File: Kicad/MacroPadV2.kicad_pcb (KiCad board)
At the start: 2 copper layers, 81 x 70 mm, 26 parts, among them K1 KSW, K10 KSW, K11 KSW, K12 KSW, K2 KSW, K3 KSW, K4 KSW, K5 KSW, K6 KSW, K7 KSW, K8 KSW, K9 KSW, SW1 RotaryEncoder_Switch, U1 SparkFunProMicro

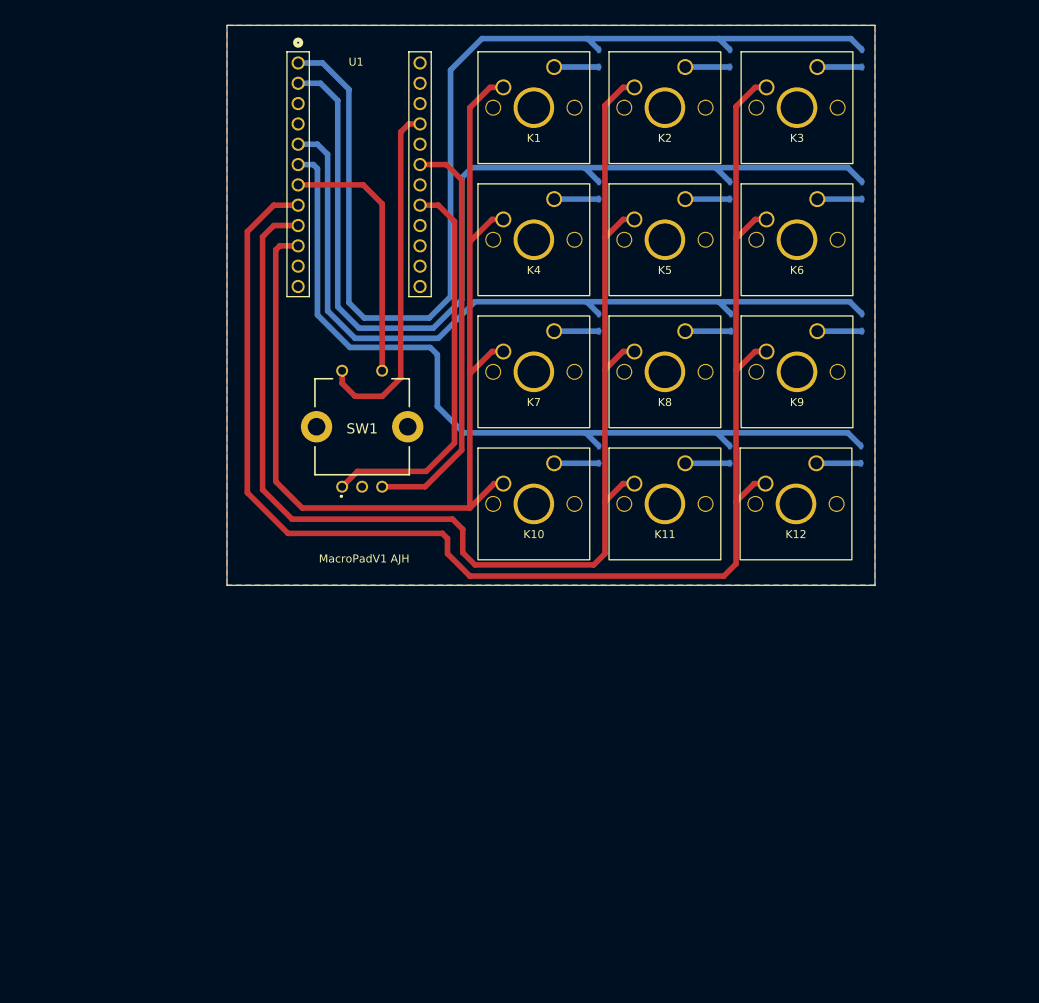
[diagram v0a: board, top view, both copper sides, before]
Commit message: Started V2 	-More space between keys(keycaps didnt fit) 	-Pull Down Resistors for Columns and Rotary Switch(ATMega32U4 is internal pull up) 	-Slightly larger board and edge holes
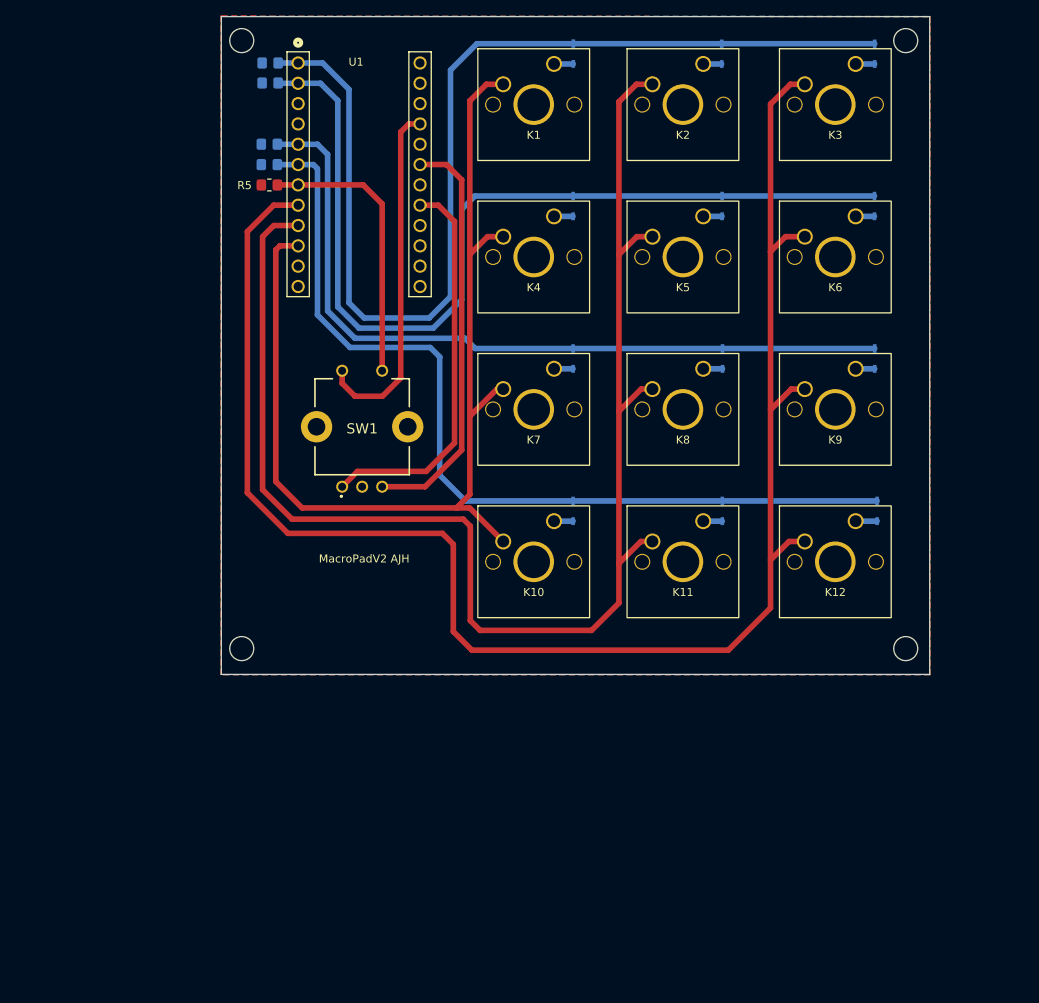
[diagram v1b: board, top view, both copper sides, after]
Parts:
- added R1: 1k, Resistor_SMD:R_0805_2012Metric_Pad1.20x1.40mm_HandSolder, B.Cu at (39.5, 26.8)
- added R2: 1k, Resistor_SMD:R_0805_2012Metric_Pad1.20x1.40mm_HandSolder, B.Cu at (39.5, 29.3)
- added R3: 1k, Resistor_SMD:R_0805_2012Metric_Pad1.20x1.40mm_HandSolder, B.Cu at (39.5, 37.0)
- added R4: 1k, Resistor_SMD:R_0805_2012Metric_Pad1.20x1.40mm_HandSolder, B.Cu at (39.5, 39.5)
- added R5: 1k, Resistor_SMD:R_0805_2012Metric_Pad1.20x1.40mm_HandSolder, F.Cu at (39.5, 42.0)
- D1, D10, D11, D12, D2, D3, D4, D5, D6, D7, D8, D9: footprint aarohanl:CR_SOD323_MCC-L -> mpadfps:sod323
- moved K12 8.75 mm to (110.2, 89.2)
- moved K11 7.58 mm to (91.2, 89.2)
- moved K10 7.24 mm to (72.5, 89.2)
- moved D10 6.82 mm to (77.4, 81.8)
- moved K9 6.71 mm to (110.2, 70.1)
- moved D12 6.34 mm to (115.4, 81.8)
- moved D11 6.09 mm to (96.1, 81.8)
- moved K6 5.25 mm to (110.2, 51.0)
- moved K8 5.21 mm to (91.2, 70.1)
- moved K3 4.81 mm to (110.2, 32.0)
- moved D7 4.74 mm to (77.4, 62.7)
- moved K7 4.70 mm to (72.5, 70.1)
- moved D9 3.82 mm to (115.1, 62.7)
- moved D8 3.63 mm to (96.1, 62.7)
- moved D1 3.58 mm to (77.5, 24.6)
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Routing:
- net ROW2: track 183.7 -> 206.5 mm
- net ROW1: track 160.1 -> 180.3 mm
- net COL3: track 104.1 -> 111.8 mm
- net COL1: track 121.2 -> 115.8 mm
- net Net-(D8-Pad2): track 5.72 -> 2.41 mm
- net Net-(D2-Pad2): track 5.59 -> 2.31 mm
- net Net-(D5-Pad2): track 5.59 -> 2.36 mm
- net Net-(D6-Pad2): track 5.59 -> 2.36 mm
- net Net-(D11-Pad2): track 5.59 -> 2.39 mm
- net Net-(D7-Pad2): track 5.59 -> 2.39 mm
- net Net-(D10-Pad2): track 5.59 -> 2.39 mm
- net Net-(D3-Pad2): track 5.59 -> 2.39 mm
- net Net-(D9-Pad2): track 5.59 -> 2.39 mm
- net Net-(D4-Pad2): track 5.59 -> 2.39 mm
- net Net-(D1-Pad2): track 5.59 -> 2.41 mm
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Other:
- board size 81 x 70 mm -> 88.5 x 82.2 mm
- board text added: "MacroPadV2 AJH"
- board text removed: "MacroPadV1 AJH"

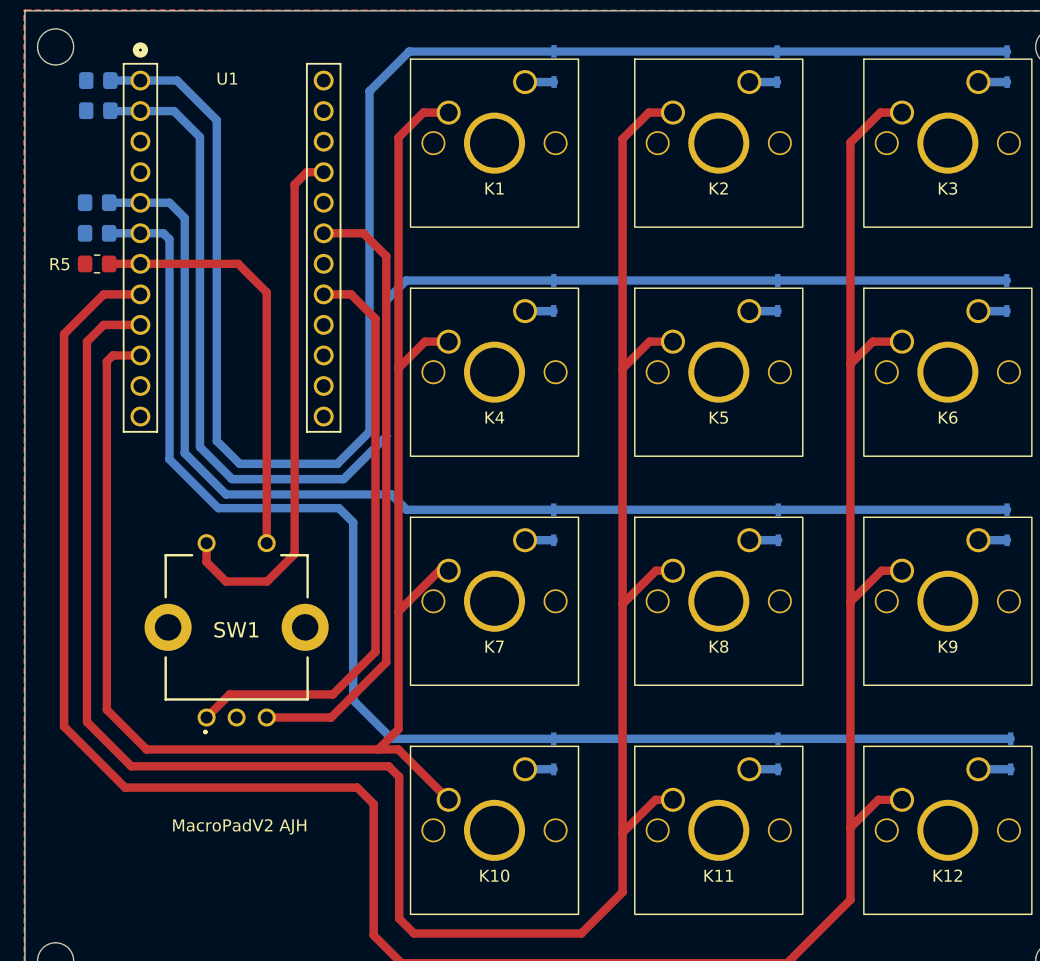
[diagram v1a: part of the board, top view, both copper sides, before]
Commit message: V2 Schem and Routing Complete for drop in micro pro, making new branch for STM32F103
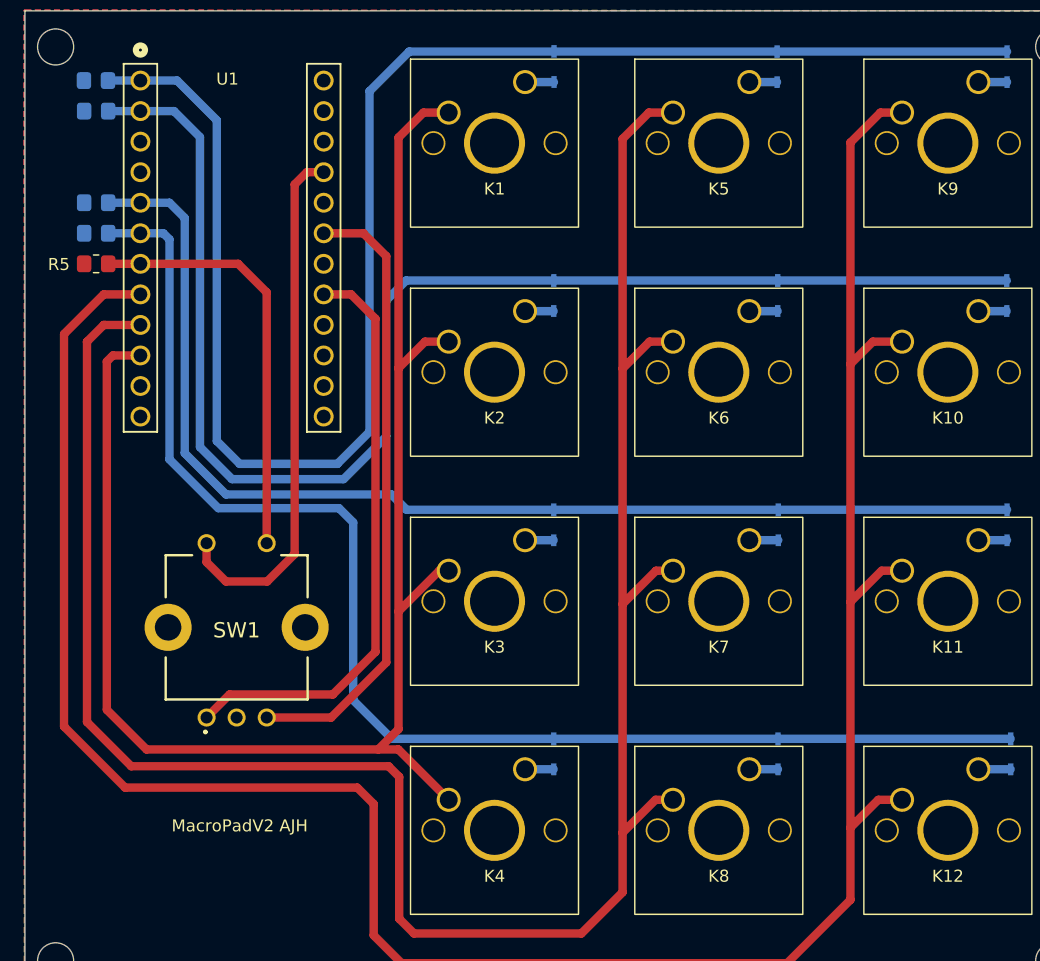
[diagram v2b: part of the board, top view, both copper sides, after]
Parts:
- moved R1 0.20 mm to (39.4, 26.8)
- moved R2 0.18 mm to (39.4, 29.3)
- moved R5 0.08 mm to (39.4, 42.0)
- moved R3 0.08 mm to (39.4, 37.0)
- moved R4 0.08 mm to (39.4, 39.5)
- renumbered D6 to D10, D9 to D11, D4 to D2, D7 to D3, D10 to D4, D2 to D5, D5 to D6, D8 to D7, D11 to D8, D3 to D9, K6 to K10, K9 to K11, K4 to K2, K7 to K3, K10 to K4, K2 to K5, K5 to K6, K8 to K7, K11 to K8, K3 to K9

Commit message: New LAyout an Routing done
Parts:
- added C1: 15pF, Capacitor_SMD:C_0805_2012Metric_Pad1.18x1.45mm_HandSolder, F.Cu at (58.5, 70.6)
- added C2: 15pF, Capacitor_SMD:C_0805_2012Metric_Pad1.18x1.45mm_HandSolder, F.Cu at (58.5, 72.8)
- added C3: 100nF, Capacitor_SMD:C_0805_2012Metric_Pad1.18x1.45mm_HandSolder, F.Cu at (52.0, 93.5)
- added C4: 100nF, Capacitor_SMD:C_0805_2012Metric_Pad1.18x1.45mm_HandSolder, F.Cu at (56.1, 65.1)
- added C5: 100nF, Capacitor_SMD:C_0805_2012Metric_Pad1.18x1.45mm_HandSolder, B.Cu at (46.2, 59.8)
- added C6: 1uF, Capacitor_SMD:C_0805_2012Metric_Pad1.18x1.45mm_HandSolder, F.Cu at (56.1, 60.7)
- added C7: 4.7uF, Capacitor_SMD:C_0805_2012Metric_Pad1.18x1.45mm_HandSolder, B.Cu at (64.2, 64.3)
- added C8: 4.7uF, Capacitor_SMD:C_0805_2012Metric_Pad1.18x1.45mm_HandSolder, F.Cu at (84.3, 56.8)
- added C9: 4.7uF, Capacitor_SMD:C_0805_2012Metric_Pad1.18x1.45mm_HandSolder, F.Cu at (70.1, 55.9)
- added D13: 1N4148WX-TP, Diode_SMD:D_0805_2012Metric_Pad1.15x1.40mm_HandSolder, B.Cu at (125.0, 65.4)
- added F1: OZCH, mpadfps:OZCHFusr, F.Cu at (68.1, 59.2)
- added J1: 3PinJump, Connector_PinHeader_2.54mm:PinHeader_1x03_P2.54mm_Vertical, F.Cu at (46.2, 63.2)
- added J2: 3PinJump, Connector_PinHeader_2.54mm:PinHeader_1x03_P2.54mm_Vertical, F.Cu at (46.2, 71.9)
- added J3: GCT-USB4085, mpadfps:USB4085-GF-A, F.Cu at (57.4, 56.5)
- added J4: 3PinJump, Connector_PinHeader_2.54mm:PinHeader_1x03_P2.54mm_Vertical, F.Cu at (70.3, 53.0)
- added J5: 4PinJump, Connector_PinHeader_2.54mm:PinHeader_1x04_P2.54mm_Vertical, F.Cu at (46.3, 80.7)
- added J6: 4PinJump, Connector_PinHeader_2.54mm:PinHeader_1x04_P2.54mm_Vertical, F.Cu at (53.0, 80.8)
- added R6: 1k, Resistor_SMD:R_0805_2012Metric_Pad1.20x1.40mm_HandSolder, B.Cu at (128.7, 122.6)
- added R7: 1k, Resistor_SMD:R_0805_2012Metric_Pad1.20x1.40mm_HandSolder, B.Cu at (128.7, 103.7)
- added R8: 1k, Resistor_SMD:R_0805_2012Metric_Pad1.20x1.40mm_HandSolder, B.Cu at (128.9, 84.4)
- added R9: 1k, Resistor_SMD:R_0805_2012Metric_Pad1.20x1.40mm_HandSolder, B.Cu at (129.5, 65.4)
- added SW2: SWITCH_TACTILE_SPST-NO_0.05A_12V, mpadfps:PTS645-G, F.Cu at (60.0, 85.0)
- added SW3: RotaryEncoder_Switch, mpadfps:PEC11H-RotaryEncoderSwitch, F.Cu at (58.1, 118.8)
- added U2: AP2114HA-3.3TRG1, keyboard_fp:SOT-223_DIO-L, F.Cu at (79.0, 55.6)
- added X1: TSX-3225_16.0000MF18X-AC6, mpadfps:TSX-3226, B.Cu at (58.5, 71.6)
- D1: value KD -> D; footprint mpadfps:sod323 -> Diode_SMD:D_0805_2012Metric_Pad1.15x1.40mm_HandSolder; moved to F.Cu
- D10, D11, D12, D2, D3, D4, D5, D6, D7, D8, D9: value KD -> 1N4148WX-TP; footprint mpadfps:sod323 -> Diode_SMD:D_0805_2012Metric_Pad1.15x1.40mm_HandSolder
- K1, K10, K11, K12, K2, K3, K4, K5, K6, K7, K8, K9: footprint aarohanl:CherryMxFP -> keyboard_fp:CherryMx
- R1, R4: value 1k -> 10k
- R2: value 1k -> 10k; moved to F.Cu
- R3: value 1k -> 5.1k; moved to F.Cu
- R5: value 1k -> 5.1k
- SW1: value RotaryEncoder_Switch -> SWITCH_TACTILE_SPST-NO_0.05A_12V; footprint aarohanl:PEC11H4020FS0016_PinCorrection -> mpadfps:PTS645-G
- U1: value SparkFunProMicro -> STM32F103C8T6TR; footprint aarohanl:SparkFrunProMicro -> mpadfps:LQFP48; moved to B.Cu
- moved D9 98.4 mm to (106.2, 122.6), turned to 90 degrees
- moved K10 82.9 mm to (80.4, 128.4)
- moved K9 77.8 mm to (118.6, 109.3)
- moved R2 65.9 mm to (54.3, 93.5), turned to 90 degrees
- moved K11 59.3 mm to (99.5, 128.4)
- moved K5 58.9 mm to (99.5, 90.3)
- moved K6 47.9 mm to (118.6, 90.3)
- moved K3 46.1 mm to (118.6, 71.2)
- moved R1 43.7 mm to (49.5, 69.3), turned to -90 degrees
- moved D11 42.1 mm to (124.9, 103.7), turned to 90 degrees
- moved D10 42.1 mm to (125.2, 84.5), turned to 90 degrees
- moved D2 42.0 mm to (87.1, 84.5), turned to 90 degrees
- moved D12 42.0 mm to (124.9, 122.7), turned to 90 degrees
- moved D4 42.0 mm to (87.1, 122.6), turned to 90 degrees
- moved D5 41.8 mm to (87.1, 65.5), turned to 90 degrees
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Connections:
- D1 pad 1: COL0 -> Net-(D1-Pad1)
- D1 pad 2: Net-(D1-Pad2) -> VBUS
- D10 pad 1: COL1 -> Net-(D10-Pad1)
- D10 pad 2: Net-(D10-Pad2) -> ROW1
- D11 pad 1: COL2 -> Net-(D11-Pad1)
- D11 pad 2: Net-(D11-Pad2) -> ROW2
- D12 pad 1: COL3 -> Net-(D12-Pad1)
- D12 pad 2: Net-(D12-Pad2) -> ROW3
- D2 pad 1: COL1 -> Net-(D2-Pad1)
- D2 pad 2: Net-(D2-Pad2) -> ROW1
- D3 pad 1: COL2 -> Net-(D3-Pad1)
- D3 pad 2: Net-(D3-Pad2) -> ROW2
- D4 pad 1: COL3 -> Net-(D4-Pad1)
- D4 pad 2: Net-(D4-Pad2) -> ROW3
- D5 pad 1: COL0 -> Net-(D5-Pad1)
- D5 pad 2: Net-(D5-Pad2) -> ROW0
- D6 pad 1: COL1 -> Net-(D6-Pad1)
- D6 pad 2: Net-(D6-Pad2) -> ROW0
- D7 pad 1: COL2 -> Net-(D7-Pad1)
- D7 pad 2: Net-(D7-Pad2) -> ROW1
- D8 pad 1: COL3 -> Net-(D8-Pad1)
- D8 pad 2: Net-(D8-Pad2) -> ROW2
- D9 pad 1: COL0 -> Net-(D9-Pad1)
- D9 pad 2: Net-(D9-Pad2) -> ROW3
- K1 pad 1: ROW0 -> COL0
- K1 pad 2: Net-(D1-Pad2) -> Net-(D5-Pad1)
- K10 pad 1: ROW2 -> COL0
- K10 pad 2: Net-(D10-Pad2) -> Net-(D4-Pad1)
- K11 pad 1: ROW2 -> COL1
- K11 pad 2: Net-(D11-Pad2) -> Net-(D9-Pad1)
- K12 pad 1: ROW2 -> COL2
- K12 pad 2: Net-(D12-Pad2) -> Net-(D12-Pad1)
- K2 pad 1: ROW0 -> COL1
- K2 pad 2: Net-(D2-Pad2) -> Net-(D6-Pad1)
- K3 pad 1: ROW0 -> COL2
- K3 pad 2: Net-(D3-Pad2) -> Net-(D13-Pad1)
- K4 pad 1: ROW0 -> COL0
- K4 pad 2: Net-(D4-Pad2) -> Net-(D2-Pad1)
- K5 pad 1: ROW1 -> COL1
- K5 pad 2: Net-(D5-Pad2) -> Net-(D7-Pad1)
- K6 pad 1: ROW1 -> COL2
- K6 pad 2: Net-(D6-Pad2) -> Net-(D10-Pad1)
- K7 pad 1: ROW1 -> COL0
- K7 pad 2: Net-(D7-Pad2) -> Net-(D3-Pad1)
- K8 pad 1: ROW1 -> COL1
- K8 pad 2: Net-(D8-Pad2) -> Net-(D8-Pad1)
- K9 pad 1: ROW2 -> COL2
- K9 pad 2: Net-(D9-Pad2) -> Net-(D11-Pad1)
- R1 pad 1: COL0 -> Net-(J1-Pad3)
- R2 pad 1: COL1 -> +3V3
- R2 pad 2: GND -> NRST
- R3 pad 1: COL2 -> GND
- R3 pad 2: GND -> Net-(J3-PadA5)
- R4 pad 1: COL3 -> Net-(J2-Pad3)
- R5 pad 1: PD4 -> GND
- R5 pad 2: GND -> Net-(J3-PadB5)
- U1 pad 1: COL0 -> +3V3
- U1 pad 11: PB4 -> ROW1
- U1 pad 12: PB5 -> ROW2
- U1 pad 13: unconnected-(U1-Pad13) -> ROW3
- U1 pad 14: GND -> COL0
- U1 pad 15: unconnected-(U1-Pad15) -> COL1
- U1 pad 16: VCC -> COL2
- U1 pad 17: PF4 -> unconnected-(U1-Pad17)
- U1 pad 18: PF6 -> MODE
- U1 pad 19: (no net) -> unconnected-(U1-Pad19)
- U1 pad 2: COL1 -> ENCSW
- U1 pad 20: PF7 -> BOOT1
- U1 pad 21: PB1 -> unconnected-(U1-Pad21)
- U1 pad 22: PB3 -> unconnected-(U1-Pad22)
- U1 pad 23: PB2 -> GND
- U1 pad 24: PB6 -> +3V3
- U1 pad 3: GND -> ENCA
- U1 pad 4: GND -> ENCB
- U1 pad 5: COL2 -> Net-(C1-Pad2)
- U1 pad 6: COL3 -> Net-(C2-Pad1)
- U1 pad 7: PD4 -> NRST
- U1 pad 8: ROW2 -> GND
- U1 pad 9: ROW1 -> +3V3
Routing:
- net ROW3: track 0.00 -> 131.8 mm
- net COL3: track 111.8 -> 0.00 mm
- net ROW2: track 206.5 -> 108.2 mm
- net GND: track 0.00 -> 95.6 mm, vias 0 -> 19
- net ROW1: track 180.3 -> 87.7 mm
- net ENCB: track 0.00 -> 84.1 mm, vias 0 -> 1
- net ENCA: track 0.00 -> 76.4 mm, vias 0 -> 1
- net NRST: track 0.00 -> 70.0 mm, vias 0 -> 1
- net ENCSW: track 0.00 -> 63.4 mm, vias 0 -> 1
- net SWCLK: track 0.00 -> 54.7 mm
- net SWDIO: track 0.00 -> 51.8 mm, vias 0 -> 1
- net PF6: track 51.6 -> 0.00 mm
- net COL2: track 96.7 -> 146.0 mm, vias 0 -> 1
- net PF7: track 49.2 -> 0.00 mm
- net VCC: track 44.1 -> 0.00 mm
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- added copper zone on In1.Cu, net +3V3
- added copper zone on In2.Cu, net GND
- removed copper zone on B.Cu, net GND
- removed copper zone on F.Cu, net GND
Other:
- board size 88.5 x 82.2 mm -> 92.8 x 91.8 mm
- copper layers 2 -> 4
- board text removed: "MacroPadV2 AJH"

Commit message: Fully Finished MacroPad V2 Schematic and Layout with stm32. Ordered and waiting for board to come in. 	-If there are no issues running the board, this should be the last commit for Kicad files. All proceeding commits should be code 	-Added gitignore with the kicad backup folder to keep backups from being added to git
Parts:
- removed the D13 at (125.0, 65.4)
- added D1: 1N4148WX-TP, Diode_SMD:D_0805_2012Metric_Pad1.15x1.40mm_HandSolder, B.Cu at (87.0, 65.4)
- added H1: M3Hole, mpadfps:M3Hole, F.Cu at (43.8, 53.5)
- added H2: M3Hole, mpadfps:M3Hole, F.Cu at (130.6, 139.2)
- added H3: M3Hole, mpadfps:M3Hole, F.Cu at (43.8, 139.2)
- added H4: M3Hole, mpadfps:M3Hole, F.Cu at (130.6, 53.5)
- added J7: 4PinJump, Connector_PinHeader_2.54mm:PinHeader_1x04_P2.54mm_Vertical, F.Cu at (98.7, 55.0)
- added R10: 10k, Resistor_SMD:R_0805_2012Metric_Pad1.20x1.40mm_HandSolder, F.Cu at (97.2, 58.0)
- added R11: 10k, Resistor_SMD:R_0805_2012Metric_Pad1.20x1.40mm_HandSolder, F.Cu at (97.2, 60.5)
- moved D9 60.3 mm to (125.4, 65.5)
- moved D7 19.2 mm to (106.3, 103.7)
- moved D6 19.1 mm to (106.5, 84.5)
- moved D8 19.1 mm to (106.3, 122.7)
- moved D5 19.1 mm to (106.2, 65.4)
- moved D3 0.46 mm to (87.2, 103.5)
- moved D2 0.35 mm to (87.5, 84.5)
- moved D4 0.30 mm to (87.4, 122.7)
- moved D11 0.22 mm to (125.1, 103.8)
- moved D12 0.11 mm to (125.0, 122.6)
- moved D10 0.10 mm to (125.2, 84.5)
- renumbered D1 to D13, K6 to K10, K9 to K11, K4 to K2, K7 to K3, K10 to K4, K2 to K5, K5 to K6, K8 to K7, K11 to K8, K3 to K9
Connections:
- D6 pad 2: ROW0 -> ROW1
- D7 pad 2: ROW1 -> ROW2
- D8 pad 2: ROW2 -> ROW3
- D9 pad 2: ROW3 -> ROW0
- K1 pad 2: Net-(D5-Pad1) -> Net-(D1-Pad1)
- K5 pad 2: Net-(D6-Pad1) -> Net-(D5-Pad1)
- K6 pad 2: Net-(D7-Pad1) -> Net-(D6-Pad1)
- K7 pad 2: Net-(D8-Pad1) -> Net-(D7-Pad1)
- K8 pad 2: Net-(D9-Pad1) -> Net-(D8-Pad1)
- K9 pad 2: Net-(D13-Pad1) (its old number) -> Net-(D9-Pad1)
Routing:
- net SCL: track 0.00 -> 43.8 mm, vias 0 -> 1
- net SDA: track 0.00 -> 40.5 mm, vias 0 -> 1
- net +3V3: track 27.5 -> 33.2 mm
- net ROW3: track 131.8 -> 127.3 mm
- net Net-(D1-Pad1): track 0.00 -> 4.19 mm
- net Net-(D13-Pad1) (its old number): track 4.03 -> 0.00 mm
- net NRST: track 70.0 -> 67.7 mm
- net ENCSW: track 63.4 -> 61.1 mm
- net ENCB: track 84.1 -> 85.7 mm
- net TraceSWO: track 43.9 -> 43.3 mm
- net ROW0: track 86.8 -> 86.2 mm
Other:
- outline, holes or cut-outs redrawn
- board text added: "BOOT0"
- board text added: "BOOT1"
- board text added: "I2C"
- board text added: "MODE"
- board text added: "MacroPadV2-AJH"
- board text added: "PROG"
- board text added: "nRST"

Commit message: Removed some backups and push for swap to desktop
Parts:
- removed J6: 4PinJump, Connector_PinHeader_2.54mm:PinHeader_1x04_P2.54mm_Vertical
- C5, C7, R1, R4, U1, X1: moved to F.Cu
- D1, D10, D11, D12, D2, D3, D4, D5, D6, D7, D8, D9: value 1N4148WX-TP -> TS4148 RBG
- J5: value 4PinJump -> 7PinHeader; footprint Connector_PinHeader_2.54mm:PinHeader_1x04_P2.54mm_Vertical -> Connector_PinHeader_2.54mm:PinHeader_1x07_P2.54mm_Vertical
- moved H2 131.5 mm to (19.4, 68.9)
- moved J7 89.8 mm to (9.18, 62.3), turned to 0 degrees
- moved SW3 79.8 mm to (19.1, 49.1)
- moved H4 76.0 mm to (55.3, 42.5)
- moved H3 70.4 mm to (29.2, 70.3)
- moved J5 53.4 mm to (9.18, 42.4)
- moved SW2 48.2 mm to (38.9, 41.6)
- moved R11 47.9 mm to (49.5, 57.2)
- moved U2 47.7 mm to (31.9, 63.3)
- moved C3 47.1 mm to (55.2, 46.6), turned to 0 degrees
- moved X1 44.4 mm to (14.3, 68.5), turned to 0 degrees
- moved C4 42.8 mm to (13.9, 72.2)
- moved SW1 40.8 mm to (27.9, 52.7)
- moved J3 40.8 mm to (16.8, 59.9), turned to 0 degrees
- moved R10 39.4 mm to (60.2, 44.5)
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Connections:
- J3 pad B6: D+ -> unconnected-(J3-PadB6)
- J3 pad B7: D- -> unconnected-(J3-PadB7)
- J3 pad SHELL: GND -> unconnected-(J3-PadSHELL)
- J5 pad 1: BOOT0 -> +3V3
- J5 pad 2: BOOT1 -> SWDIO/JTMS
- J5 pad 3: TraceSWO -> SWCLK/JTCK
- J5 pad 4: NRST -> JTDI
- U1 pad 34: unconnected-(U1-Pad34) -> SWDIO/JTMS
- U1 pad 37: SWDIO -> SWCLK/JTCK
- U1 pad 38: SWCLK -> JTDI
- U1 pad 39: TraceSWO -> JTDO
- U1 pad 40: unconnected-(U1-Pad40) -> JTNRST
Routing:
- net COL2: track 146.0 -> 0.00 mm, vias 1 -> 0
- net ROW3: track 127.3 -> 0.04 mm
- net COL1: track 126.3 -> 0.00 mm, vias 1 -> 0
- net ROW2: track 108.2 -> 0.28 mm
- net COL0: track 103.7 -> 0.00 mm, vias 1 -> 0
- net GND: track 95.6 -> 1.45 mm, vias 19 -> 1
- net ROW1: track 87.7 -> 0.11 mm
- net ROW0: track 86.2 -> 0.04 mm
- net ENCB: track 85.7 -> 0.00 mm, vias 1 -> 0
- net ENCA: track 76.4 -> 0.00 mm, vias 1 -> 0
- net NRST: track 67.7 -> 0.00 mm, vias 1 -> 0
- net ENCSW: track 61.1 -> 0.00 mm, vias 1 -> 0
- net SWCLK: track 54.7 -> 0.00 mm
- net SWDIO: track 51.8 -> 0.00 mm, vias 1 -> 0
- net SCL: track 43.8 -> 0.00 mm, vias 1 -> 0
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- removed copper zone on In1.Cu, net +3V3
- removed copper zone on In2.Cu, net GND
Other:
- board outline removed
- board text added: "MacroPadV3-AJH"
- board text removed: "BOOT0"
- board text removed: "BOOT1"
- board text removed: "I2C"
- board text removed: "MODE"
- board text removed: "MacroPadV2-AJH"
- board text removed: "PROG"
- board text removed: "nRST"
